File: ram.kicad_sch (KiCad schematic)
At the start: 1 part

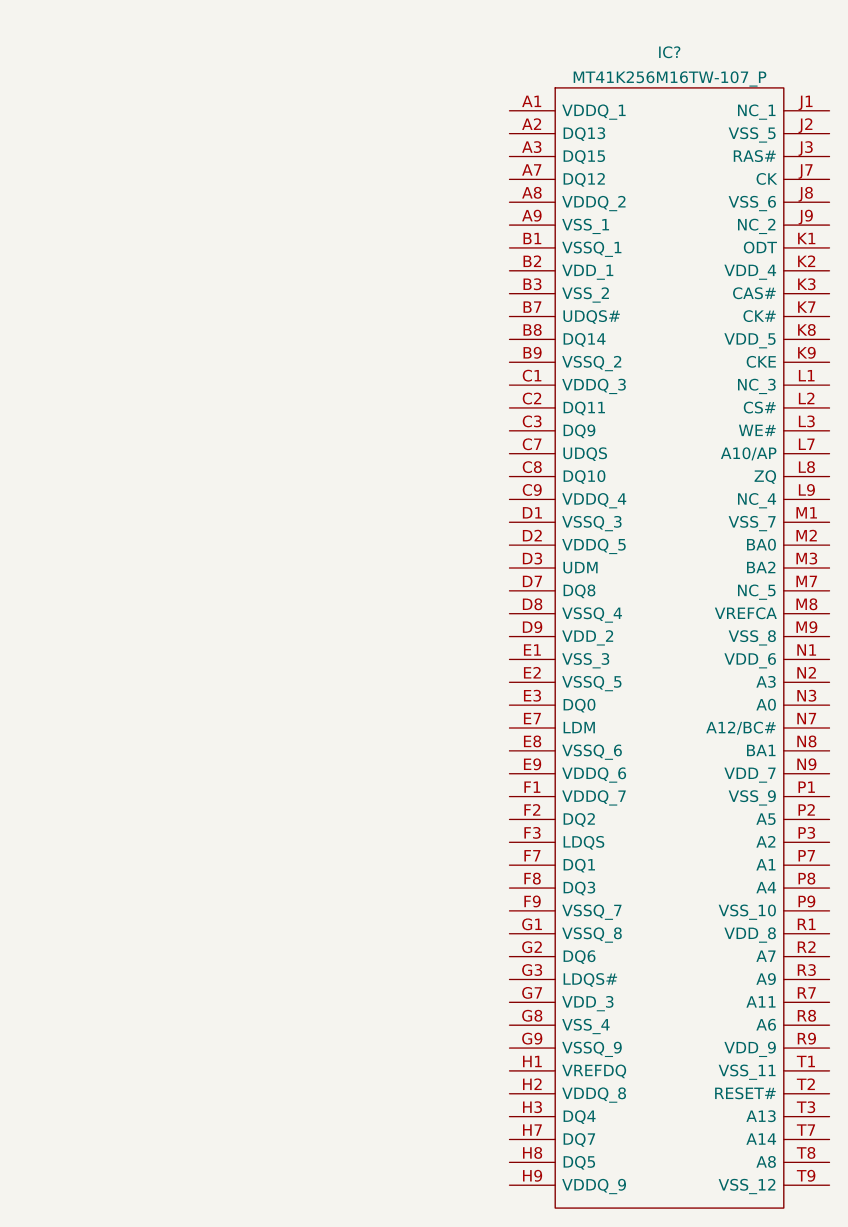
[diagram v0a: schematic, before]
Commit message: Change Symbols / Footprintst to local library
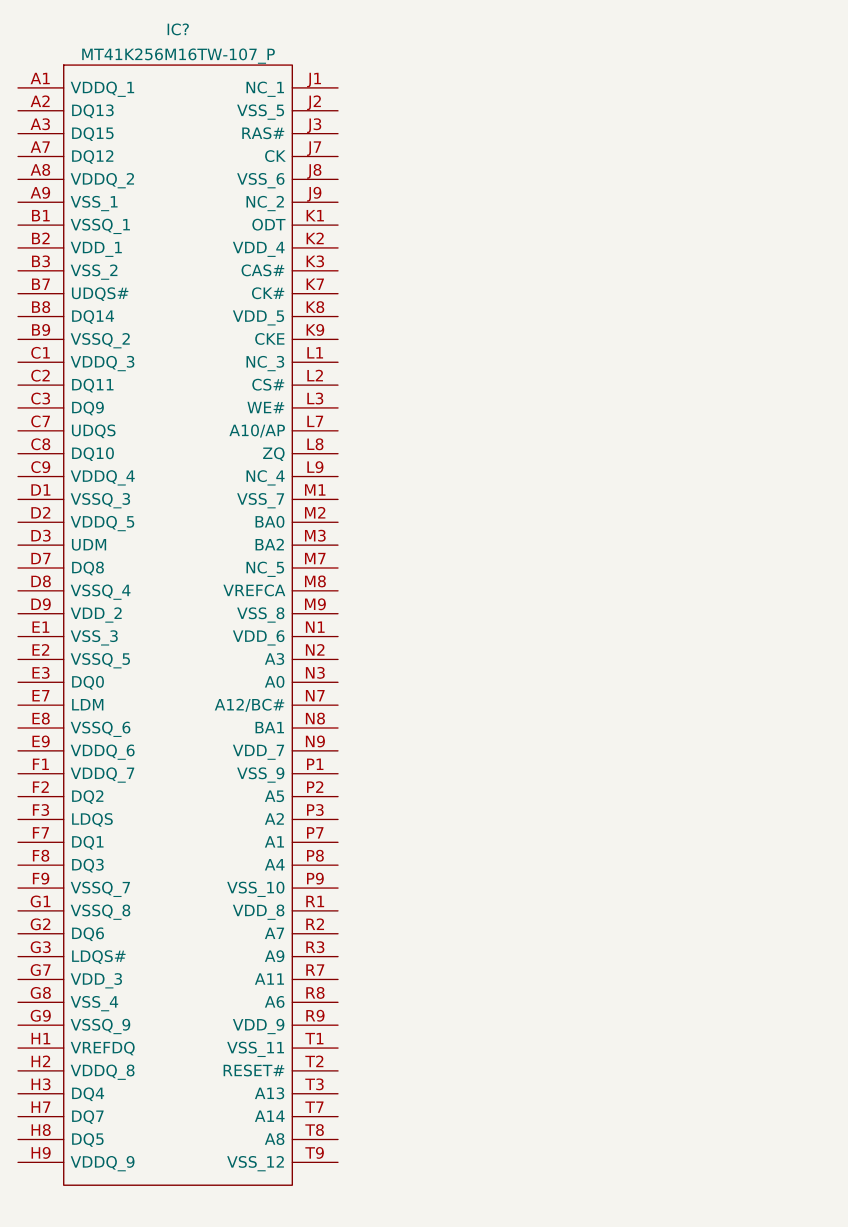
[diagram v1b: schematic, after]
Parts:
- removed IC?: MT41K256M16TW-107_P, BGA96C80P9X16_800X1400X120, symbol SamacSys_Parts:MT41K256M16TW-107_P
- added IC?: MT41K256M16TW-107_P, BGA96C80P9X16_800X1400X120, symbol mp1lib:MT41K256M16TW-107_P
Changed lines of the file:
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@@
 (kicad_sch (version 20211123) (generator eeschema)
   (paper "A4")
-  (symbol (lib_id "SamacSys_Parts:MT41K256M16TW-107_P") (at 87.63 35.56 0) (unit 1)
+  (symbol (lib_id "mp1lib:MT41K256M16TW-107_P") (at 33.02 33.02 0) (unit 1)
     (in_bom yes) (on_board yes) (fields_autoplaced)
-    (property "Reference" "IC?" (id 0) (at 105.41 29.1043 0))
-    (property "Value" "MT41K256M16TW-107_P" (id 1) (at 105.41 31.8794 0))
-    (property "Footprint" "BGA96C80P9X16_800X1400X120" (id 2) (at 119.38 33.02 0)
+    (property "Reference" "IC?" (id 0) (at 50.8 26.5643 0))
+    (property "Value" "MT41K256M16TW-107_P" (id 1) (at 50.8 29.3394 0))
+    (property "Footprint" "BGA96C80P9X16_800X1400X120" (id 2) (at 64.77 30.48 0)
       (effects (font (size 1.27 1.27)) (justify left) hide)
     )
-    (property "Datasheet" "https://datasheet.datasheetarchive.com/originals/distributors/DKDS42/DSANUWW0045409.pdf" (id 3) (at 119.38 35.56 0)
+    (property "Datasheet" "https://datasheet.datasheetarchive.com/originals/distributors/DKDS42/DSANUWW0045409.pdf" (id 3) (at 64.77 33.02 0)
       (effects (font (size 1.27 1.27)) (justify left) hide)
     )
-    (property "Description" "MICRON - MT41K256M16TW-107:P - SDRAM, 256M X 16BIT, 0 TO 95DEG C" (id 4) (at 119.38 38.1 0)
+    (property "Description" "MICRON - MT41K256M16TW-107:P - SDRAM, 256M X 16BIT, 0 TO 95DEG C" (id 4) (at 64.77 35.56 0)
       (effects (font (size 1.27 1.27)) (justify left) hide)
     )
-    (property "Height" "1.2" (id 5) (at 119.38 40.64 0)
+    (property "Height" "1.2" (id 5) (at 64.77 38.1 0)
       (effects (font (size 1.27 1.27)) (justify left) hide)
     )
-    (property "Manufacturer_Name" "Micron" (id 6) (at 119.38 43.18 0)
+    (property "Manufacturer_Name" "Micron" (id 6) (at 64.77 40.64 0)
       (effects (font (size 1.27 1.27)) (justify left) hide)
     )
-    (property "Manufacturer_Part_Number" "MT41K256M16TW-107:P" (id 7) (at 119.38 45.72 0)
+    (property "Manufacturer_Part_Number" "MT41K256M16TW-107:P" (id 7) (at 64.77 43.18 0)
       (effects (font (size 1.27 1.27)) (justify left) hide)
     )
-    (property "Mouser Part Number" "340-265846-TRAY" (id 8) (at 119.38 48.26 0)
+    (property "Mouser Part Number" "340-265846-TRAY" (id 8) (at 64.77 45.72 0)
       (effects (font (size 1.27 1.27)) (justify left) hide)
     )
-    (property "Mouser Price/Stock" "https://www.mouser.co.uk/ProductDetail/Micron/MT41K256M16TW-107P?qs=rrS6PyfT74eHnbmAfGvzkQ%3D%3D" (id 9) (at 119.38 50.8 0)
+    (property "Mouser Price/Stock" "https://www.mouser.co.uk/ProductDetail/Micron/MT41K256M16TW-107P?qs=rrS6PyfT74eHnbmAfGvzkQ%3D%3D" (id 9) (at 64.77 48.26 0)
       (effects (font (size 1.27 1.27)) (justify left) hide)
     )
-    (property "Arrow Part Number" "MT41K256M16TW-107:P" (id 10) (at 119.38 53.34 0)
+    (property "Arrow Part Number" "MT41K256M16TW-107:P" (id 10) (at 64.77 50.8 0)
       (effects (font (size 1.27 1.27)) (justify left) hide)
     )
-    (property "Arrow Price/Stock" "https://www.arrow.com/en/products/mt41k256m16tw-107p/micron-technology" (id 11) (at 119.38 55.88 0)
+    (property "Arrow Price/Stock" "https://www.arrow.com/en/products/mt41k256m16tw-107p/micron-technology" (id 11) (at 64.77 53.34 0)
       (effects (font (size 1.27 1.27)) (justify left) hide)
     )
-    (property "Mouser Testing Part Number" "" (id 12) (at 119.38 58.42 0)
+    (property "Mouser Testing Part Number" "" (id 12) (at 64.77 55.88 0)
       (effects (font (size 1.27 1.27)) (justify left) hide)
     )
-    (property "Mouser Testing Price/Stock" "" (id 13) (at 119.38 60.96 0)
+    (property "Mouser Testing Price/Stock" "" (id 13) (at 64.77 58.42 0)
       (effects (font (size 1.27 1.27)) (justify left) hide)
     )

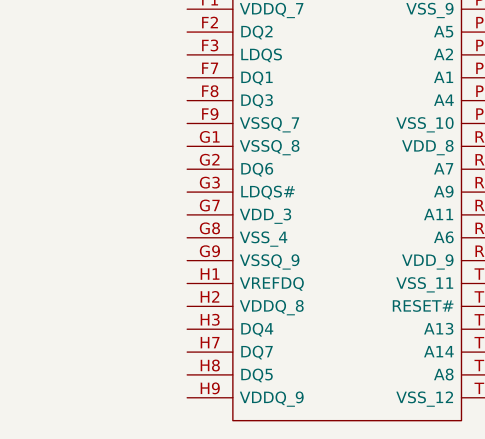
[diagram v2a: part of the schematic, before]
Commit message: added VREV_DDR
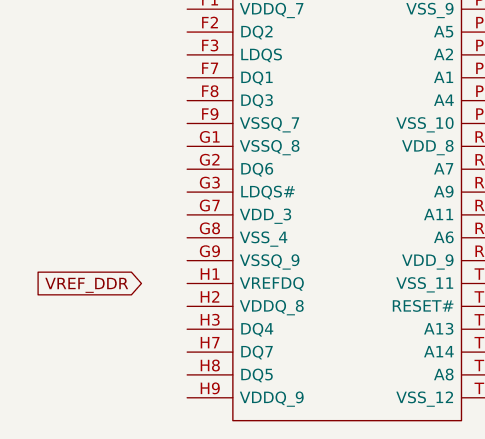
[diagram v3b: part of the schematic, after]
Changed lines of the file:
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@@
 (kicad_sch (version 20230121) (generator eeschema)
   (paper "A4")
+  (global_label "VREF_DDR" (shape input) (at 27.94 139.7 180) (fields_autoplaced)
+    (effects (font (size 1.27 1.27)) (justify right))
+    (property "Intersheetrefs" "${INTERSHEET_REFS}" (at 15.6604 139.7 0)
+      (effects (font (size 1.27 1.27)) (justify right) hide)
+    )
+  )
   (symbol (lib_id "mp1lib:MT41K256M16TW-107_P") (at 33.02 33.02 0) (unit 1)
     (in_bom yes) (on_board yes) (dnp no) (fields_autoplaced)

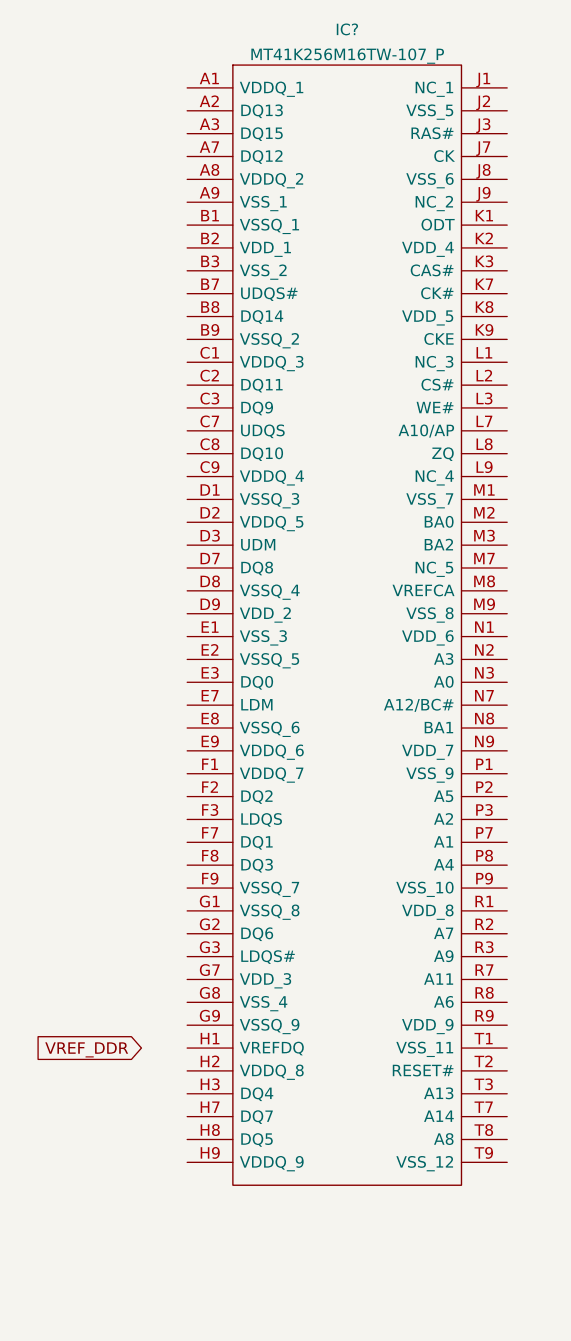
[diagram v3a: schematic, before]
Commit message: Updated Symbols + Added Supply connections
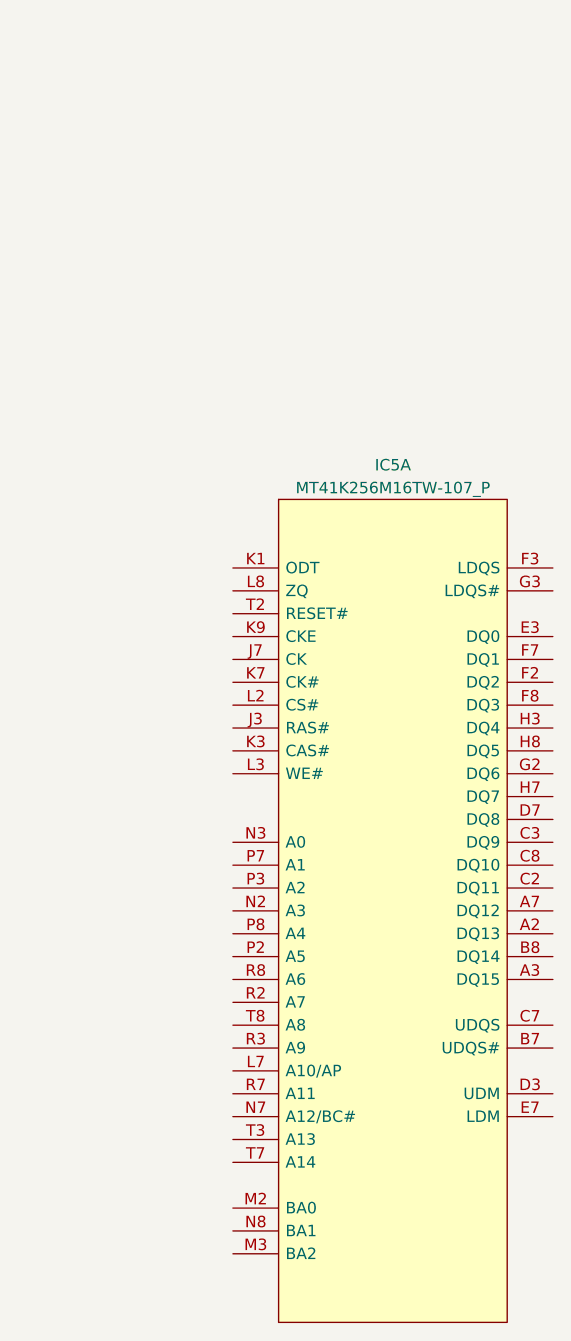
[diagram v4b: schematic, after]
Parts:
- removed IC?: MT41K256M16TW-107_P, BGA96C80P9X16_800X1400X120, symbol mp1lib:MT41K256M16TW-107_P
- added IC5: MT41K256M16TW-107_P, ARMband:BGA96C80P9X16_800X1400X120, symbol ARMband:MT41K256M16TW-107_P
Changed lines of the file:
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@@
 (kicad_sch (version 20230121) (generator eeschema)
   (paper "A4")
-  (global_label "VREF_DDR" (shape input) (at 27.94 139.7 180) (fields_autoplaced)
-    (effects (font (size 1.27 1.27)) (justify right))
-    (property "Intersheetrefs" "${INTERSHEET_REFS}" (at 15.6604 139.7 0)
-      (effects (font (size 1.27 1.27)) (justify right) hide)
-    )
-  )
-  (symbol (lib_id "mp1lib:MT41K256M16TW-107_P") (at 33.02 33.02 0) (unit 1)
+  (symbol (lib_name "MT41K256M16TW-107_P_1") (lib_id "ARMband:MT41K256M16TW-107_P") (at 38.1 81.28 0) (unit 1)
     (in_bom yes) (on_board yes) (dnp no) (fields_autoplaced)
-    (property "Reference" "IC?" (at 50.8 26.5643 0)
+    (property "Reference" "IC5" (at 55.88 74.93 0)
       (effects (font (size 1.27 1.27)))
     )
-    (property "Value" "MT41K256M16TW-107_P" (at 50.8 29.3394 0)
+    (property "Value" "MT41K256M16TW-107_P" (at 55.88 77.47 0)
       (effects (font (size 1.27 1.27)))
     )
-    (property "Footprint" "BGA96C80P9X16_800X1400X120" (at 64.77 30.48 0)
+    (property "Footprint" "ARMband:BGA96C80P9X16_800X1400X120" (at 104.775 80.645 0)
       (effects (font (size 1.27 1.27)) (justify left) hide)
     )
-    (property "Datasheet" "https://datasheet.datasheetarchive.com/originals/distributors/DKDS42/DSANUWW0045409.pdf" (at 64.77 33.02 0)
+    (property "Datasheet" "https://datasheet.datasheetarchive.com/originals/distributors/DKDS42/DSANUWW0045409.pdf" (at 104.775 83.185 0)
       (effects (font (size 1.27 1.27)) (justify left) hide)
     )
-    (property "Description" "MICRON - MT41K256M16TW-107:P - SDRAM, 256M X 16BIT, 0 TO 95DEG C" (at 64.77 35.56 0)
+    (property "Description" "MICRON - MT41K256M16TW-107:P - SDRAM, 256M X 16BIT, 0 TO 95DEG C" (at 104.775 85.725 0)
       (effects (font (size 1.27 1.27)) (justify left) hide)
     )
-    (property "Height" "1.2" (at 64.77 38.1 0)
+    (property "Height" "1.2" (at 106.68 105.41 0)
       (effects (font (size 1.27 1.27)) (justify left) hide)
     )
-    (property "Manufacturer_Name" "Micron" (at 64.77 40.64 0)
+    (property "Mouser Part Number" "340-265846-TRAY" (at 104.775 90.805 0)
       (effects (font (size 1.27 1.27)) (justify left) hide)
     )
-    (property "Manufacturer_Part_Number" "MT41K256M16TW-107:P" (at 64.77 43.18 0)
+    (property "Mouser Price/Stock" "https://www.mouser.co.uk/ProductDetail/Micron/MT41K256M16TW-107P?qs=rrS6PyfT74eHnbmAfGvzkQ%3D%3D" (at 104.775 93.345 0)
       (effects (font (size 1.27 1.27)) (justify left) hide)
     )
-    (property "Mouser Part Number" "340-265846-TRAY" (at 64.77 45.72 0)
+    (property "Manufacturer_Name" "Micron" (at 104.775 95.885 0)
       (effects (font (size 1.27 1.27)) (justify left) hide)
     )
-    (property "Mouser Price/Stock" "https://www.mouser.co.uk/ProductDetail/Micron/MT41K256M16TW-107P?qs=rrS6PyfT74eHnbmAfGvzkQ%3D%3D" (at 64.77 48.26 0)
+    (property "Manufacturer_Part_Number" "MT41K256M16TW-107:P" (at 104.775 98.425 0)
       (effects (font (size 1.27 1.27)) (justify left) hide)
     )
-    (property "Arrow Part Number" "MT41K256M16TW-107:P" (at 64.77 50.8 0)
-      (effects (font (size 1.27 1.27)) (justify left) hide)
+    (property "MFN" "" (at 38.1 81.28 0)
+      (effects (font (size 1.27 1.27)) hide)
     )
-    (property "Arrow Price/Stock" "https://www.arrow.com/en/products/mt41k256m16tw-107p/micron-technology" (at 64.77 53.34 0)
-      (effects (font (size 1.27 1.27)) (justify left) hide)
-    )
-    (property "Mouser Testing Part Number" "" (at 64.77 55.88 0)
-      (effects (font (size 1.27 1.27)) (justify left) hide)
-    )
-    (property "Mouser Testing Price/Stock" "" (at 64.77 58.42 0)
-      (effects (font (size 1.27 1.27)) (justify left) hide)
-    )
-    (pin "A1")
     (pin "A2")
     (pin "A3")
     (pin "A7")
-    (pin "A8")
-    (pin "A9")
-    (pin "B1")
-    (pin "B2")
-    (pin "B3")
     (pin "B7")
     (pin "B8")
-    (pin "B9")
-    (pin "C1")
     (pin "C2")
     (pin "C3")
     (pin "C7")
     (pin "C8")
-    (pin "C9")
-    (pin "D1")
-    (pin "D2")
     (pin "D3")
     (pin "D7")
-    (pin "D8")
-    (pin "D9")
-    (pin "E1")
-    (pin "E2")
     (pin "E3")
     (pin "E7")
-    (pin "E8")
-    (pin "E9")
-    (pin "F1")
     (pin "F2")
     (pin "F3")
     (pin "F7")
     (pin "F8")
-    (pin "F9")
-    (pin "G1")
     (pin "G2")
     (pin "G3")
-    (pin "G7")
-    (pin "G8")
-    (pin "G9")
-    (pin "H1")
-    (pin "H2")
     (pin "H3")
     (pin "H7")
     (pin "H8")
-    (pin "H9")
     (pin "J1")
-    (pin "J2")
     (pin "J3")
     (pin "J7")
-    (pin "J8")
     (pin "J9")
     (pin "K1")
-    (pin "K2")
     (pin "K3")
     (pin "K7")
-    (pin "K8")
     (pin "K9")
     (pin "L1")
@@
     (pin "L8")
     (pin "L9")
-    (pin "M1")
     (pin "M2")
     (pin "M3")
     (pin "M7")
-    (pin "M8")
-    (pin "M9")
-    (pin "N1")
     (pin "N2")
     (pin "N3")
     (pin "N7")
     (pin "N8")
-    (pin "N9")
-    (pin "P1")
     (pin "P2")
     (pin "P3")
     (pin "P7")
     (pin "P8")
-    (pin "P9")
-    (pin "R1")
     (pin "R2")
     (pin "R3")
     (pin "R7")
     (pin "R8")
-    (pin "R9")
-    (pin "T1")
     (pin "T2")
     (pin "T3")
     (pin "T7")
     (pin "T8")
+    (pin "A1")
+    (pin "A8")
+    (pin "A9")
+    (pin "B1")
+    (pin "B2")
+    (pin "B3")
+    (pin "B9")
+    (pin "C1")
+    (pin "C9")
+    (pin "D1")
+    (pin "D2")
+    (pin "D8")
+    (pin "D9")
+    (pin "E1")
+    (pin "E2")
+    (pin "E8")
+    (pin "E9")
+    (pin "F1")
+    (pin "F9")
+    (pin "G1")
+    (pin "G7")
+    (pin "G8")
+    (pin "G9")
+    (pin "H1")
+    (pin "H2")
+    (pin "H9")
+    (pin "J2")
+    (pin "J8")
+    (pin "K2")
+    (pin "K8")
+    (pin "M1")
+    (pin "M8")
+    (pin "M9")
+    (pin "N1")
+    (pin "N9")
+    (pin "P1")
+    (pin "P9")
+    (pin "R1")
+    (pin "R9")
+    (pin "T1")
     (pin "T9")
     (instances
       (project "gba"
         (path "/017c50c6-333c-4d31-ad5a-278994a09b14/f5831ad7-86f4-4338-9d6c-a9943f11383a"
-          (reference "IC?") (unit 1)
+          (reference "IC5") (unit 1)
         )
       )
